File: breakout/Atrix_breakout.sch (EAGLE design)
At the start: 9 parts

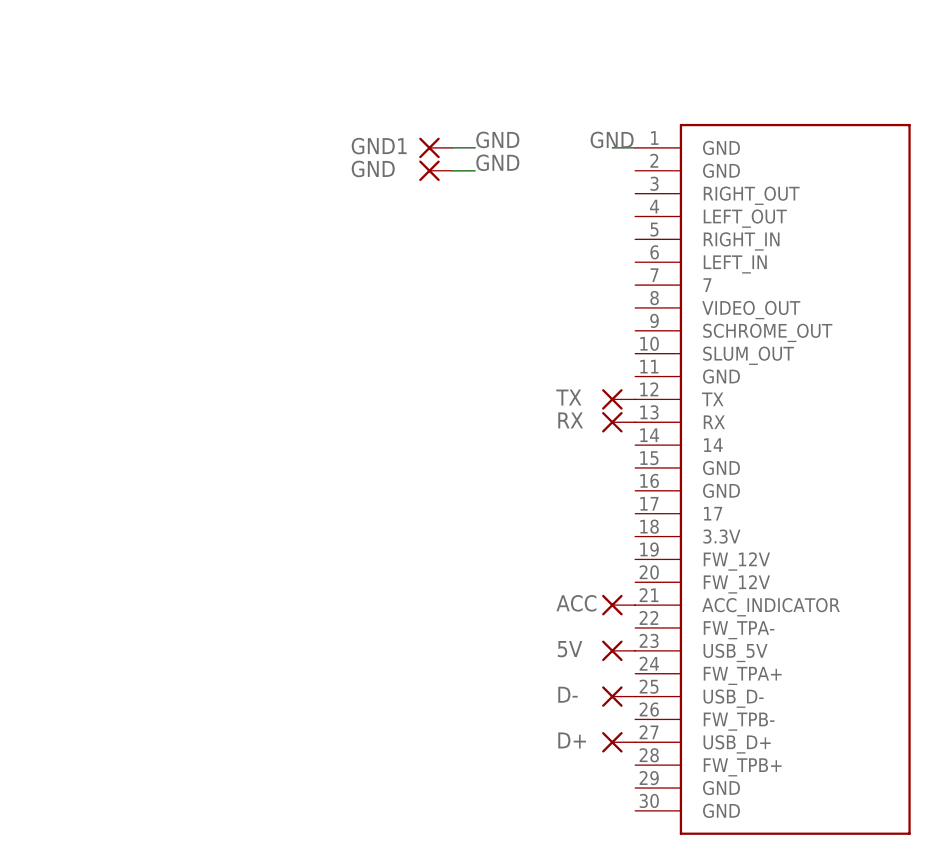
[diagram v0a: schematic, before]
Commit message: Breakout updated to v1.0.1, improved board. See rev.txt
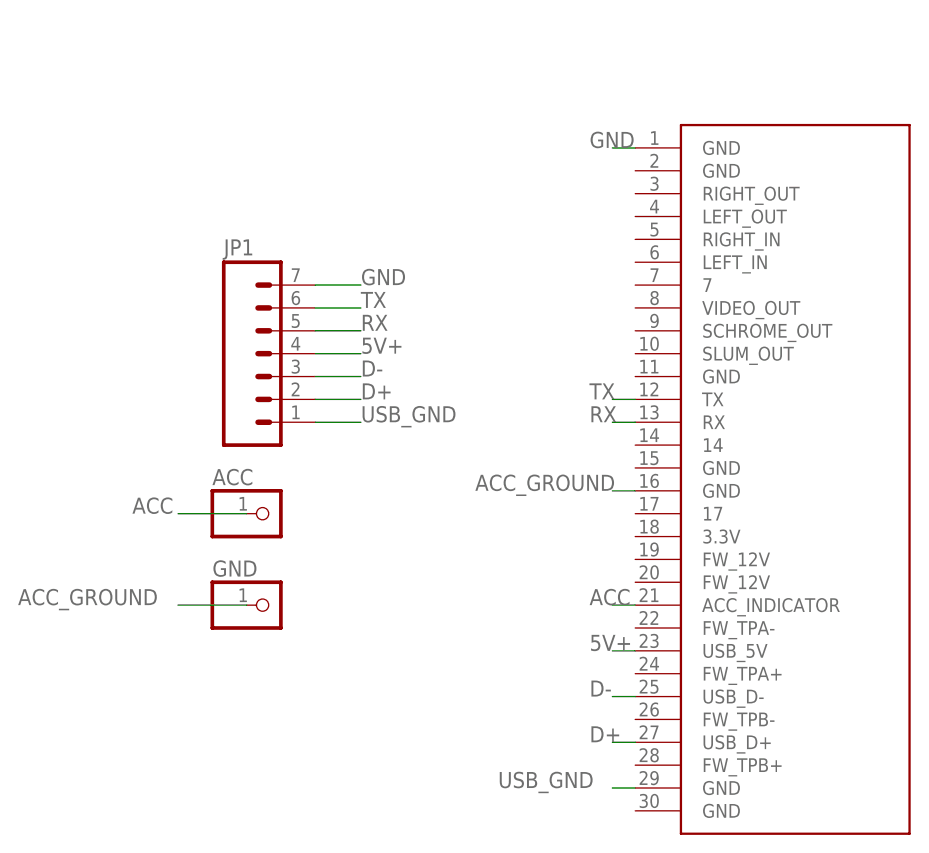
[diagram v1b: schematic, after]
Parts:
- removed 5V, D+, D-, GND1, RX, TX: (no value), wirepad:1,6/0,8
- added JP1: (no value), SparkFun-Connectors:M07
- ACC, GND: device wirepad:1,6/0,8 -> adafruit:PINHD-1X1
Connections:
- removed net N$2: ACC.P, U$1.ACC_INDICATOR
- removed net N$3: D-.P, U$1.USB_D-
- removed net N$4: D+.P, U$1.USB_D+
- removed net N$6: RX.P, U$1.RX
- removed net N$7: TX.P, U$1.TX
- removed net N$8: 5V.P, U$1.USB_5V
- new net 5V+: JP1.4, U$1.USB_5V
- new net ACC: ACC.1, U$1.ACC_INDICATOR
- new net ACC_GROUND: GND.1, U$1.GND@16
- new net D+: JP1.2, U$1.USB_D+
- new net D-: JP1.3, U$1.USB_D-
- new net RX: JP1.5, U$1.RX
- new net TX: JP1.6, U$1.TX
- new net USB_GND: JP1.1, U$1.GND@29
- net GND: now also JP1.7; no longer GND.P, GND1.P
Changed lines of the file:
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@@
 <layer number="113" name="IDFDebug" color="4" fill="1" visible="yes" active="yes"/>
 <layer number="116" name="Patch_BOT" color="9" fill="4" visible="yes" active="yes"/>
+<layer number="118" name="Rect_Pads" color="7" fill="1" visible="no" active="no"/>
 <layer number="121" name="_tsilk" color="7" fill="1" visible="yes" active="yes"/>
 <layer number="122" name="_bsilk" color="7" fill="1" visible="yes" active="yes"/>
@@
 <layer number="223" name="223bmp" color="24" fill="1" visible="no" active="no"/>
 <layer number="224" name="224bmp" color="25" fill="1" visible="no" active="no"/>
+<layer number="231" name="Eagle3D_PG1" color="7" fill="1" visible="no" active="no"/>
+<layer number="232" name="Eagle3D_PG2" color="7" fill="1" visible="no" active="no"/>
+<layer number="233" name="Eagle3D_PG3" color="7" fill="1" visible="no" active="no"/>
 <layer number="248" name="Housing" color="7" fill="1" visible="yes" active="yes"/>
 <layer number="249" name="Edge" color="7" fill="1" visible="yes" active="yes"/>
@@
 <parts>
 <part name="U$1" library="SparkFun-Connectors" deviceset="IPOD_CONNECTOR_MALE" device=""/>
-<part name="GND" library="wirepad" deviceset="1,6/0,8" device=""/>
-<part name="D-" library="wirepad" deviceset="1,6/0,8" device=""/>
-<part name="D+" library="wirepad" deviceset="1,6/0,8" device=""/>
-<part name="RX" library="wirepad" deviceset="1,6/0,8" device=""/>
-<part name="TX" library="wirepad" deviceset="1,6/0,8" device=""/>
-<part name="5V" library="wirepad" deviceset="1,6/0,8" device=""/>
-<part name="ACC" library="wirepad" deviceset="1,6/0,8" device=""/>
-<part name="GND1" library="wirepad" deviceset="1,6/0,8" device=""/>
+<part name="JP1" library="SparkFun-Connectors" deviceset="M07" device=""/>
+<part name="ACC" library="adafruit" deviceset="PINHD-1X1" device=""/>
+<part name="GND" library="adafruit" deviceset="PINHD-1X1" device=""/>
 </parts>
 <sheets>
@@
 <instances>
 <instance part="U$1" gate="G$1" x="134.62" y="45.72"/>
-<instance part="GND" gate="P" x="93.98" y="78.74" smashed="yes">
-<attribute name="NAME" x="85.217" y="78.0542" size="1.778" layer="95"/>
-<attribute name="VALUE" x="92.837" y="75.438" size="1.778" layer="96"/>
-</instance>
-<instance part="D-" gate="P" x="114.3" y="20.32" smashed="yes">
-<attribute name="NAME" x="108.077" y="19.6342" size="1.778" layer="95"/>
-<attribute name="VALUE" x="113.157" y="17.018" size="1.778" layer="96"/>
-</instance>
-<instance part="D+" gate="P" x="114.3" y="15.24" smashed="yes">
-<attribute name="NAME" x="108.077" y="14.5542" size="1.778" layer="95"/>
-<attribute name="VALUE" x="113.157" y="11.938" size="1.778" layer="96"/>
-</instance>
-<instance part="RX" gate="P" x="114.3" y="50.8" smashed="yes">
-<attribute name="NAME" x="108.077" y="50.1142" size="1.778" layer="95"/>
-<attribute name="VALUE" x="113.157" y="47.498" size="1.778" layer="96"/>
-</instance>
-<instance part="TX" gate="P" x="114.3" y="53.34" smashed="yes">
-<attribute name="NAME" x="108.077" y="52.6542" size="1.778" layer="95"/>
-<attribute name="VALUE" x="113.157" y="50.038" size="1.778" layer="96"/>
-</instance>
-<instance part="5V" gate="P" x="114.3" y="25.4" smashed="yes">
-<attribute name="NAME" x="108.077" y="24.7142" size="1.778" layer="95"/>
-<attribute name="VALUE" x="113.157" y="22.098" size="1.778" layer="96"/>
-</instance>
-<instance part="ACC" gate="P" x="114.3" y="30.48" smashed="yes">
-<attribute name="NAME" x="108.077" y="29.7942" size="1.778" layer="95"/>
-<attribute name="VALUE" x="113.157" y="27.178" size="1.778" layer="96"/>
-</instance>
-<instance part="GND1" gate="P" x="93.98" y="81.28" smashed="yes">
-<attribute name="NAME" x="85.217" y="80.5942" size="1.778" layer="95"/>
-<attribute name="VALUE" x="92.837" y="77.978" size="1.778" layer="96"/>
-</instance>
+<instance part="JP1" gate="G$1" x="76.2" y="55.88"/>
+<instance part="ACC" gate="G$1" x="76.2" y="40.64"/>
+<instance part="GND" gate="G$1" x="76.2" y="30.48"/>
 </instances>
 <busses>
 </busses>
 <nets>
-<net name="N$3" class="0">
-<segment>
-<pinref part="U$1" gate="G$1" pin="USB_D-"/>
-<pinref part="D-" gate="P" pin="P"/>
-</segment>
-</net>
-<net name="N$4" class="0">
-<segment>
-<pinref part="U$1" gate="G$1" pin="USB_D+"/>
-<pinref part="D+" gate="P" pin="P"/>
-</segment>
-</net>
-<net name="N$6" class="0">
-<segment>
-<pinref part="U$1" gate="G$1" pin="RX"/>
-<pinref part="RX" gate="P" pin="P"/>
-</segment>
-</net>
-<net name="N$7" class="0">
-<segment>
-<pinref part="U$1" gate="G$1" pin="TX"/>
-<pinref part="TX" gate="P" pin="P"/>
-</segment>
-</net>
-<net name="N$8" class="0">
-<segment>
-<pinref part="U$1" gate="G$1" pin="USB_5V"/>
-<pinref part="5V" gate="P" pin="P"/>
-</segment>
-</net>
-<net name="N$2" class="0">
-<segment>
-<pinref part="U$1" gate="G$1" pin="ACC_INDICATOR"/>
-<pinref part="ACC" gate="P" pin="P"/>
-</segment>
-</net>
 <net name="GND" class="0">
 <segment>
@@
 </segment>
 <segment>
-<pinref part="GND1" gate="P" pin="P"/>
-<wire x1="96.52" y1="81.28" x2="99.06" y2="81.28" width="0.1524" layer="91"/>
-<label x="99.06" y="81.28" size="1.778" layer="95"/>
+<pinref part="JP1" gate="G$1" pin="7"/>
+<wire x1="81.28" y1="66.04" x2="86.36" y2="66.04" width="0.1524" layer="91"/>
+<label x="86.36" y="66.04" size="1.778" layer="95"/>
+</segment>
+</net>
+<net name="TX" class="0">
+<segment>
+<pinref part="U$1" gate="G$1" pin="TX"/>
+<wire x1="116.84" y1="53.34" x2="114.3" y2="53.34" width="0.1524" layer="91"/>
+<label x="111.76" y="53.34" size="1.778" layer="95"/>
 </segment>
 <segment>
-<pinref part="GND" gate="P" pin="P"/>
-<wire x1="96.52" y1="78.74" x2="99.06" y2="78.74" width="0.1524" layer="91"/>
-<label x="99.06" y="78.74" size="1.778" layer="95"/>
+<pinref part="JP1" gate="G$1" pin="6"/>
+<wire x1="81.28" y1="63.5" x2="86.36" y2="63.5" width="0.1524" layer="91"/>
+<label x="86.36" y="63.5" size="1.778" layer="95"/>
 </segment>
 </net>
+<net name="RX" class="0">
+<segment>
+<pinref part="U$1" gate="G$1" pin="RX"/>
+<wire x1="116.84" y1="50.8" x2="114.3" y2="50.8" width="0.1524" layer="91"/>
+<label x="111.76" y="50.8" size="1.778" layer="95"/>
+</segment>
+<segment>
+<pinref part="JP1" gate="G$1" pin="5"/>
+<wire x1="81.28" y1="60.96" x2="86.36" y2="60.96" width="0.1524" layer="91"/>
+<label x="86.36" y="60.96" size="1.778" layer="95"/>
+</segment>
+</net>
+<net name="ACC" class="0">
+<segment>
+<pinref part="U$1" gate="G$1" pin="ACC_INDICATOR"/>
+<wire x1="116.84" y1="30.48" x2="114.3" y2="30.48" width="0.1524" layer="91"/>
+<label x="111.76" y="30.48" size="1.778" layer="95"/>
+</segment>
+<segment>
+<pinref part="ACC" gate="G$1" pin="1"/>
+<wire x1="73.66" y1="40.64" x2="66.04" y2="40.64" width="0.1524" layer="91"/>
+<label x="60.96" y="40.64" size="1.778" layer="95"/>
+</segment>
+</net>
+<net name="5V+" class="0">
+<segment>
+<pinref part="U$1" gate="G$1" pin="USB_5V"/>
+<wire x1="116.84" y1="25.4" x2="114.3" y2="25.4" width="0.1524" layer="91"/>
+<label x="111.76" y="25.4" size="1.778" layer="95"/>
+</segment>
+<segment>
+<pinref part="JP1" gate="G$1" pin="4"/>
+<wire x1="81.28" y1="58.42" x2="86.36" y2="58.42" width="0.1524" layer="91"/>
+<label x="86.36" y="58.42" size="1.778" layer="95"/>
+</segment>
+</net>
+<net name="D-" class="0">
+<segment>
+<pinref part="U$1" gate="G$1" pin="USB_D-"/>
+<wire x1="116.84" y1="20.32" x2="114.3" y2="20.32" width="0.1524" layer="91"/>
+<label x="111.76" y="20.32" size="1.778" layer="95"/>
+</segment>
+<segment>
+<pinref part="JP1" gate="G$1" pin="3"/>
+<wire x1="81.28" y1="55.88" x2="86.36" y2="55.88" width="0.1524" layer="91"/>
+<label x="86.36" y="55.88" size="1.778" layer="95"/>
+</segment>
+</net>
+<net name="D+" class="0">
+<segment>
+<pinref part="U$1" gate="G$1" pin="USB_D+"/>
+<wire x1="116.84" y1="15.24" x2="114.3" y2="15.24" width="0.1524" layer="91"/>
+<label x="111.76" y="15.24" size="1.778" layer="95"/>
+</segment>
+<segment>
+<pinref part="JP1" gate="G$1" pin="2"/>
+<wire x1="81.28" y1="53.34" x2="86.36" y2="53.34" width="0.1524" layer="91"/>
+<label x="86.36" y="53.34" size="1.778" layer="95"/>
+</segment>
+</net>
+<net name="USB_GND" class="0">
+<segment>
+<pinref part="JP1" gate="G$1" pin="1"/>
+<wire x1="81.28" y1="50.8" x2="86.36" y2="50.8" width="0.1524" layer="91"/>
+<label x="86.36" y="50.8" size="1.778" layer="95"/>
+</segment>
+<segment>
+<pinref part="U$1" gate="G$1" pin="GND@29"/>
+<wire x1="116.84" y1="10.16" x2="114.3" y2="10.16" width="0.1524" layer="91"/>
+<label x="101.6" y="10.16" size="1.778" layer="95"/>
+</segment>
+</net>
+<net name="ACC_GROUND" class="0">
+<segment>
+<pinref part="U$1" gate="G$1" pin="GND@16"/>
+<wire x1="116.84" y1="43.18" x2="114.3" y2="43.18" width="0.1524" layer="91"/>
+<label x="99.06" y="43.18" size="1.778" layer="95"/>
+</segment>
+<segment>
+<pinref part="GND" gate="G$1" pin="1"/>
+<wire x1="73.66" y1="30.48" x2="66.04" y2="30.48" width="0.1524" layer="91"/>
+<label x="48.26" y="30.48" size="1.778" layer="95"/>
+</segment>
+</net>

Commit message: Rev v1.0.2r2
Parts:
- removed ACC, GND: (no value), adafruit:PINHD-1X1
- added R1: (no value), eagle-ltspice:R0207/10
- added U$3: USB-MINIB-5PIN, SparkFun-Connectors:USB-MINIB-5PIN
- JP1: device SparkFun-Connectors:M07 -> con-amp-quick:M03
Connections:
- net 5V+: now also U$3.VBUS; no longer JP1.4
- net ACC: now also R1.2; no longer ACC.1
- net ACC_GROUND: now also R1.1; no longer GND.1
- net D+: now also U$3.D+; no longer JP1.2
- net D-: now also U$3.D-; no longer JP1.3
- net GND: now also JP1.3; no longer JP1.7
- net RX: now also JP1.1; no longer JP1.5
- net TX: now also JP1.2; no longer JP1.6
- net USB_GND: now also U$3.GND; no longer JP1.1
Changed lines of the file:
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@@
 <layers>
 <layer number="1" name="Top" color="4" fill="1" visible="no" active="no"/>
+<layer number="2" name="Route2" color="1" fill="3" visible="no" active="no"/>
+<layer number="3" name="Route3" color="4" fill="3" visible="no" active="no"/>
+<layer number="4" name="Route4" color="1" fill="4" visible="no" active="no"/>
+<layer number="5" name="Route5" color="4" fill="4" visible="no" active="no"/>
+<layer number="6" name="Route6" color="1" fill="8" visible="no" active="no"/>
+<layer number="7" name="Route7" color="4" fill="8" visible="no" active="no"/>
+<layer number="8" name="Route8" color="1" fill="2" visible="no" active="no"/>
+<layer number="9" name="Route9" color="4" fill="2" visible="no" active="no"/>
+<layer number="10" name="Route10" color="1" fill="7" visible="no" active="no"/>
+<layer number="11" name="Route11" color="4" fill="7" visible="no" active="no"/>
+<layer number="12" name="Route12" color="1" fill="5" visible="no" active="no"/>
+<layer number="13" name="Route13" color="4" fill="5" visible="no" active="no"/>
+<layer number="14" name="Route14" color="1" fill="6" visible="no" active="no"/>
+<layer number="15" name="Route15" color="4" fill="6" visible="no" active="no"/>
 <layer number="16" name="Bottom" color="1" fill="1" visible="no" active="no"/>
 <layer number="17" name="Pads" color="2" fill="1" visible="no" active="no"/>
@@
 <layer number="56" name="wert" color="7" fill="1" visible="no" active="no"/>
 <layer number="57" name="tCAD" color="7" fill="1" visible="no" active="no"/>
+<layer number="59" name="tCarbon" color="7" fill="1" visible="no" active="no"/>
+<layer number="60" name="bCarbon" color="7" fill="1" visible="no" active="no"/>
 <layer number="90" name="Modules" color="5" fill="1" visible="yes" active="yes"/>
 <layer number="91" name="Nets" color="2" fill="1" visible="yes" active="yes"/>
@@
 <layer number="127" name="_tValues" color="7" fill="1" visible="yes" active="yes"/>
 <layer number="128" name="_bValues" color="7" fill="1" visible="yes" active="yes"/>
+<layer number="129" name="Mask" color="7" fill="1" visible="yes" active="yes"/>
 <layer number="131" name="tAdjust" color="7" fill="1" visible="yes" active="yes"/>
 <layer number="132" name="bAdjust" color="7" fill="1" visible="yes" active="yes"/>
@@
 <layer number="223" name="223bmp" color="24" fill="1" visible="no" active="no"/>
 <layer number="224" name="224bmp" color="25" fill="1" visible="no" active="no"/>
+<layer number="225" name="225bmp" color="7" fill="1" visible="yes" active="yes"/>
+<layer number="226" name="226bmp" color="7" fill="1" visible="yes" active="yes"/>
+<layer number="227" name="227bmp" color="7" fill="1" visible="yes" active="yes"/>
+<layer number="228" name="228bmp" color="7" fill="1" visible="yes" active="yes"/>
+<layer number="229" name="229bmp" color="7" fill="1" visible="yes" active="yes"/>
+<layer number="230" name="230bmp" color="7" fill="1" visible="yes" active="yes"/>
 <layer number="231" name="Eagle3D_PG1" color="7" fill="1" visible="no" active="no"/>
 <layer number="232" name="Eagle3D_PG2" color="7" fill="1" visible="no" active="no"/>
@@
 <layer number="251" name="SMDround" color="12" fill="11" visible="no" active="no"/>
 <layer number="254" name="cooling" color="7" fill="1" visible="yes" active="yes"/>
+<layer number="255" name="routoute" color="7" fill="1" visible="yes" active="yes"/>
 </layers>
 <schematic xreflabel="%F%N/%S.%C%R" xrefpart="/%S.%C%R">
@@
 <parts>
 <part name="U$1" library="SparkFun-Connectors" deviceset="IPOD_CONNECTOR_MALE" device=""/>
-<part name="JP1" library="SparkFun-Connectors" deviceset="M07" device=""/>
-<part name="ACC" library="adafruit" deviceset="PINHD-1X1" device=""/>
-<part name="GND" library="adafruit" deviceset="PINHD-1X1" device=""/>
+<part name="JP1" library="con-amp-quick" deviceset="M03" device=""/>
+<part name="U$3" library="SparkFun-Connectors" deviceset="USB-MINIB" device="-5PIN"/>
+<part name="R1" library="eagle-ltspice" deviceset="R" device="0207/10"/>
 </parts>
 <sheets>
@@
 <instance part="U$1" gate="G$1" x="134.62" y="45.72"/>
 <instance part="JP1" gate="G$1" x="76.2" y="55.88"/>
-<instance part="ACC" gate="G$1" x="76.2" y="40.64"/>
-<instance part="GND" gate="G$1" x="76.2" y="30.48"/>
+<instance part="U$3" gate="G$1" x="81.28" y="86.36" rot="R180"/>
+<instance part="R1" gate="G$1" x="53.34" y="45.72" rot="R90"/>
 </instances>
 <busses>
@@
 </segment>
 <segment>
-<pinref part="JP1" gate="G$1" pin="7"/>
-<wire x1="81.28" y1="66.04" x2="86.36" y2="66.04" width="0.1524" layer="91"/>
-<label x="86.36" y="66.04" size="1.778" layer="95"/>
+<pinref part="JP1" gate="G$1" pin="3"/>
+<wire x1="83.82" y1="58.42" x2="86.36" y2="58.42" width="0.1524" layer="91"/>
+<label x="86.36" y="58.42" size="1.778" layer="95"/>
 </segment>
 </net>
@@
 </segment>
 <segment>
-<pinref part="JP1" gate="G$1" pin="6"/>
-<wire x1="81.28" y1="63.5" x2="86.36" y2="63.5" width="0.1524" layer="91"/>
-<label x="86.36" y="63.5" size="1.778" layer="95"/>
+<pinref part="JP1" gate="G$1" pin="2"/>
+<wire x1="83.82" y1="55.88" x2="86.36" y2="55.88" width="0.1524" layer="91"/>
+<label x="86.36" y="55.88" size="1.778" layer="95"/>
 </segment>
 </net>
@@
 </segment>
 <segment>
-<pinref part="JP1" gate="G$1" pin="5"/>
-<wire x1="81.28" y1="60.96" x2="86.36" y2="60.96" width="0.1524" layer="91"/>
-<label x="86.36" y="60.96" size="1.778" layer="95"/>
+<pinref part="JP1" gate="G$1" pin="1"/>
+<wire x1="83.82" y1="53.34" x2="86.36" y2="53.34" width="0.1524" layer="91"/>
+<label x="86.36" y="53.34" size="1.778" layer="95"/>
 </segment>
 </net>
@@
 </segment>
 <segment>
-<pinref part="ACC" gate="G$1" pin="1"/>
-<wire x1="73.66" y1="40.64" x2="66.04" y2="40.64" width="0.1524" layer="91"/>
-<label x="60.96" y="40.64" size="1.778" layer="95"/>
+<pinref part="R1" gate="G$1" pin="2"/>
+<wire x1="53.34" y1="50.8" x2="53.34" y2="55.88" width="0.1524" layer="91"/>
+<label x="53.34" y="55.88" size="1.778" layer="95"/>
 </segment>
 </net>
@@
 </segment>
 <segment>
-<pinref part="JP1" gate="G$1" pin="4"/>
-<wire x1="81.28" y1="58.42" x2="86.36" y2="58.42" width="0.1524" layer="91"/>
-<label x="86.36" y="58.42" size="1.778" layer="95"/>
+<pinref part="U$3" gate="G$1" pin="VBUS"/>
+<wire x1="83.82" y1="76.2" x2="88.9" y2="76.2" width="0.1524" layer="91"/>
+<label x="88.9" y="76.2" size="1.778" layer="95"/>
 </segment>
 </net>
@@
 </segment>
 <segment>
-<pinref part="JP1" gate="G$1" pin="3"/>
-<wire x1="81.28" y1="55.88" x2="86.36" y2="55.88" width="0.1524" layer="91"/>
-<label x="86.36" y="55.88" size="1.778" layer="95"/>
+<pinref part="U$3" gate="G$1" pin="D-"/>
+<wire x1="83.82" y1="78.74" x2="88.9" y2="78.74" width="0.1524" layer="91"/>
+<label x="88.9" y="78.74" size="1.778" layer="95"/>
 </segment>
 </net>
@@
 </segment>
 <segment>
-<pinref part="JP1" gate="G$1" pin="2"/>
-<wire x1="81.28" y1="53.34" x2="86.36" y2="53.34" width="0.1524" layer="91"/>
-<label x="86.36" y="53.34" size="1.778" layer="95"/>
+<pinref part="U$3" gate="G$1" pin="D+"/>
+<wire x1="83.82" y1="81.28" x2="88.9" y2="81.28" width="0.1524" layer="91"/>
+<label x="88.9" y="81.28" size="1.778" layer="95"/>
 </segment>
 </net>
 <net name="USB_GND" class="0">
-<segment>
-<pinref part="JP1" gate="G$1" pin="1"/>
-<wire x1="81.28" y1="50.8" x2="86.36" y2="50.8" width="0.1524" layer="91"/>
-<label x="86.36" y="50.8" size="1.778" layer="95"/>
-</segment>
 <segment>
 <pinref part="U$1" gate="G$1" pin="GND@29"/>
@@
 <label x="101.6" y="10.16" size="1.778" layer="95"/>
 </segment>
+<segment>
+<pinref part="U$3" gate="G$1" pin="GND"/>
+<wire x1="83.82" y1="86.36" x2="88.9" y2="86.36" width="0.1524" layer="91"/>
+<label x="88.9" y="86.36" size="1.778" layer="95"/>
+</segment>
 </net>
 <net name="ACC_GROUND" class="0">
@@
 </segment>
 <segment>
-<pinref part="GND" gate="G$1" pin="1"/>
-<wire x1="73.66" y1="30.48" x2="66.04" y2="30.48" width="0.1524" layer="91"/>
-<label x="48.26" y="30.48" size="1.778" layer="95"/>
-</segment>
-</net>
+<pinref part="R1" gate="G$1" pin="1"/>
+<wire x1="53.34" y1="40.64" x2="53.34" y2="35.56" width="0.1524" layer="91"/>
+<label x="53.34" y="35.56" size="1.778" layer="95"/>
+</segment>
+</net>
